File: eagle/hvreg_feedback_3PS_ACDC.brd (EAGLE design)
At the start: 128.5 x 101.9 mm, 14 parts

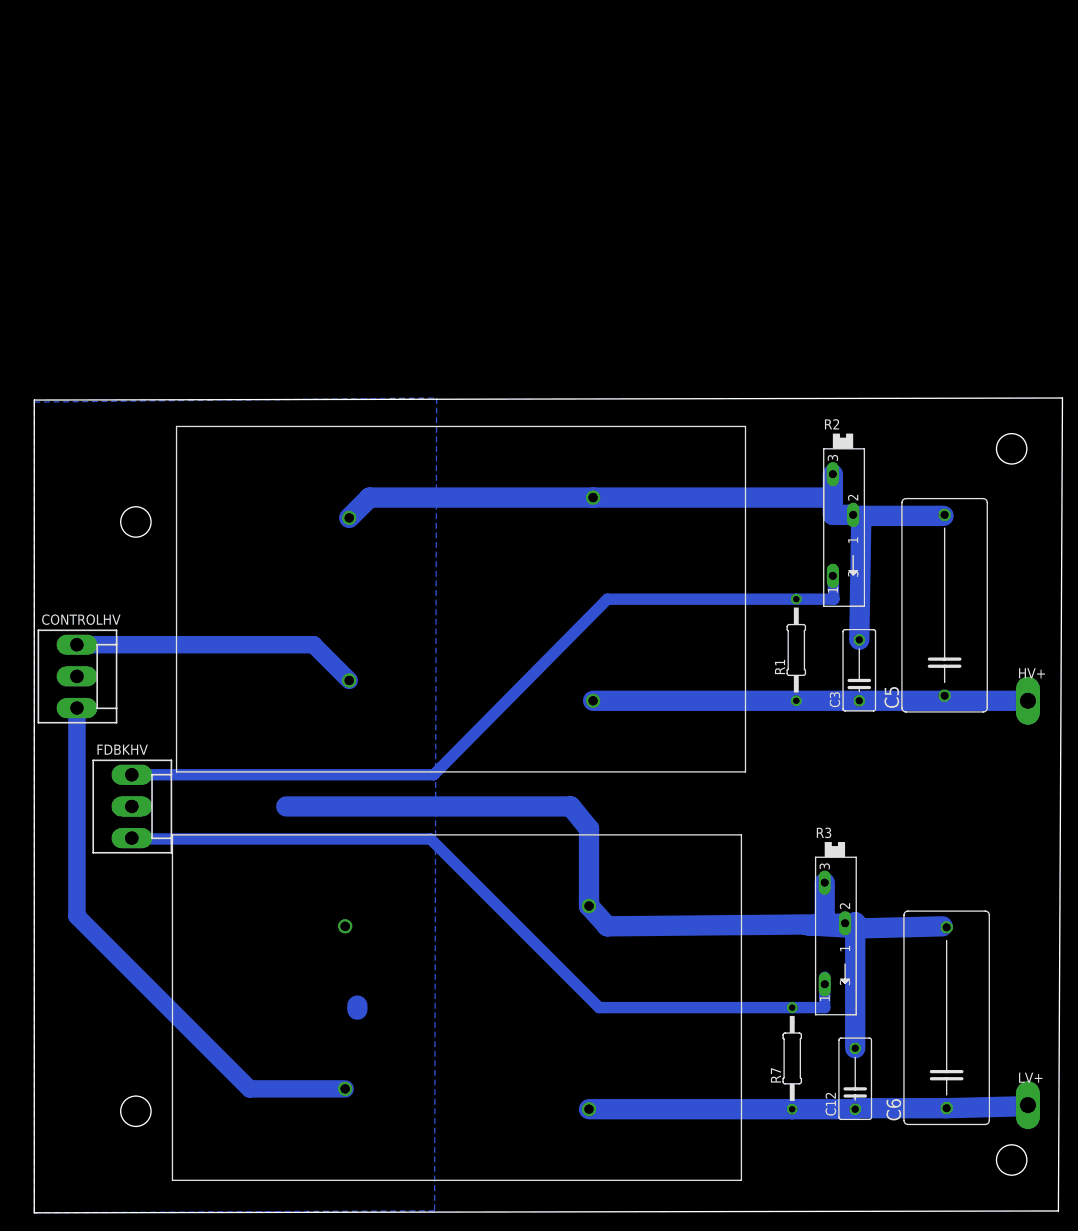
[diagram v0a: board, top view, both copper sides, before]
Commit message: 3PS, 2 1kV in parallel
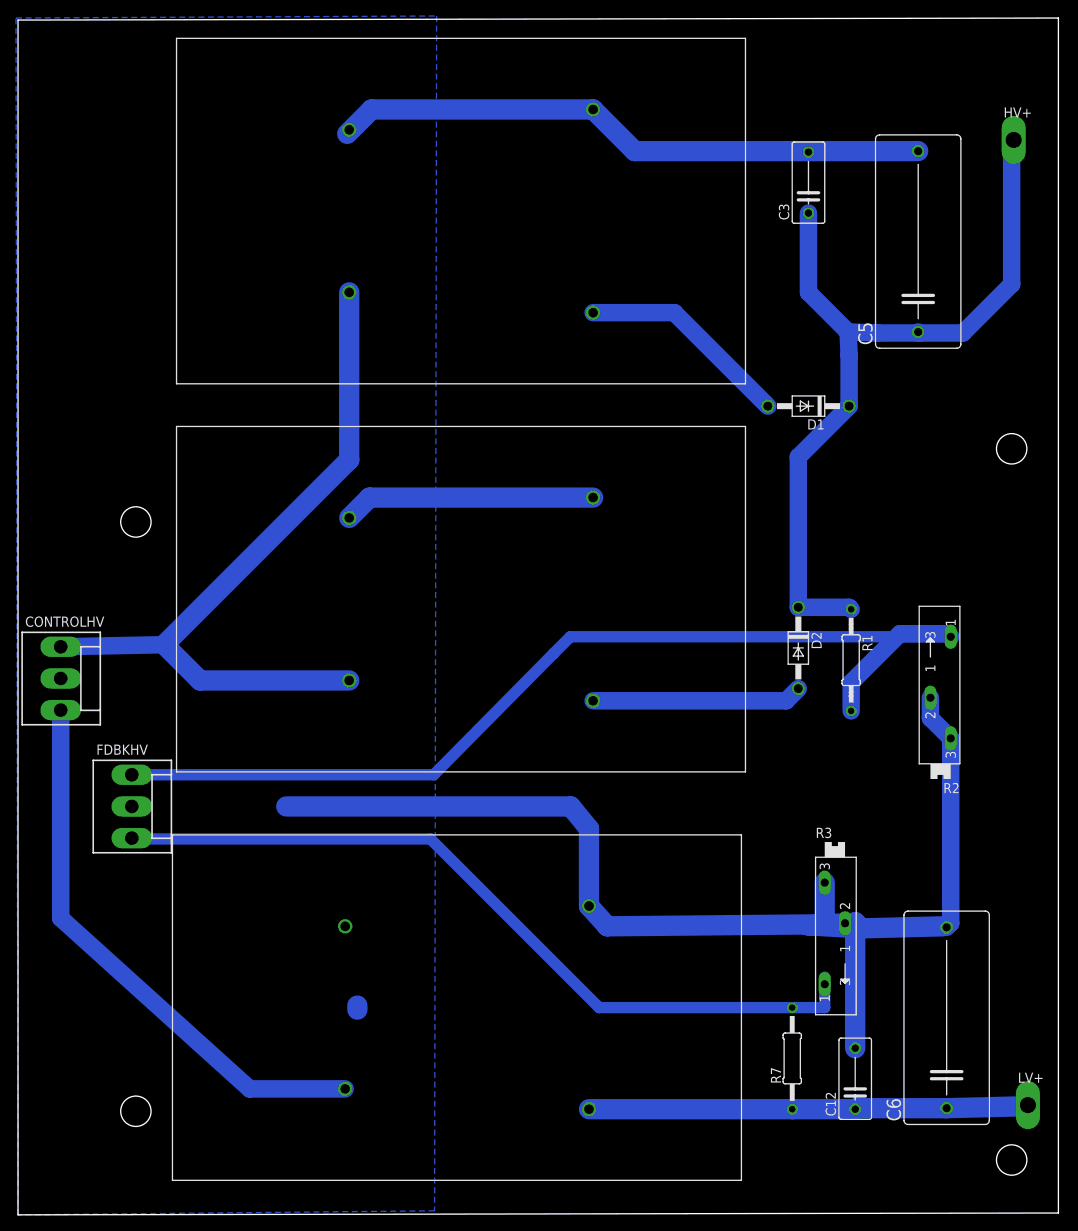
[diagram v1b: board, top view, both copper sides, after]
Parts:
- added D1, D2: 1N4004, diode:DO41-10
- added U$3: EMCO-F104PIN, dc-dc-converter:EMCO-F
- moved HV+ 70.1 mm to (140.2, 133.9)
- moved C3 61.3 mm to (114.6, 128.5)
- moved C5 45.6 mm to (128.3, 121.2)
- moved R2 22.6 mm to (131.1, 66.0), turned to 90 degrees
- moved R1 6.97 mm to (119.9, 68.8), turned to 270 degrees
- moved CONTROLHV 2.05 mm to (21.1, 66.5)
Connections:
- removed net N$1: C3.1, C5.1, HV+.TP, R1.1, U$1.P$3
- new net N$6: D1.A, U$3.P$3
- new net N$7: D2.A, U$1.P$3
- new net N$9: C3.1, C5.1, D1.C, D2.C, HV+.TP, R1.1
- net GND: now also U$3.P$2, U$3.P$4
- net N$4: now also U$3.P$1
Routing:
- net N$9: track 0.00 -> 101.3 mm
- net N$4: track 35.9 -> 91.5 mm
- net N$1: track 54.4 -> 0.00 mm
- net GND: track 222.6 -> 262.7 mm
- net N$3: track 99.8 -> 128.2 mm
- net N$6: track 0.00 -> 26.7 mm
- net N$7: track 0.00 -> 26.3 mm
- net N$5: track 68.5 -> 69.8 mm
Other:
- board size 128.5 x 101.9 mm -> 130 x 149.6 mm

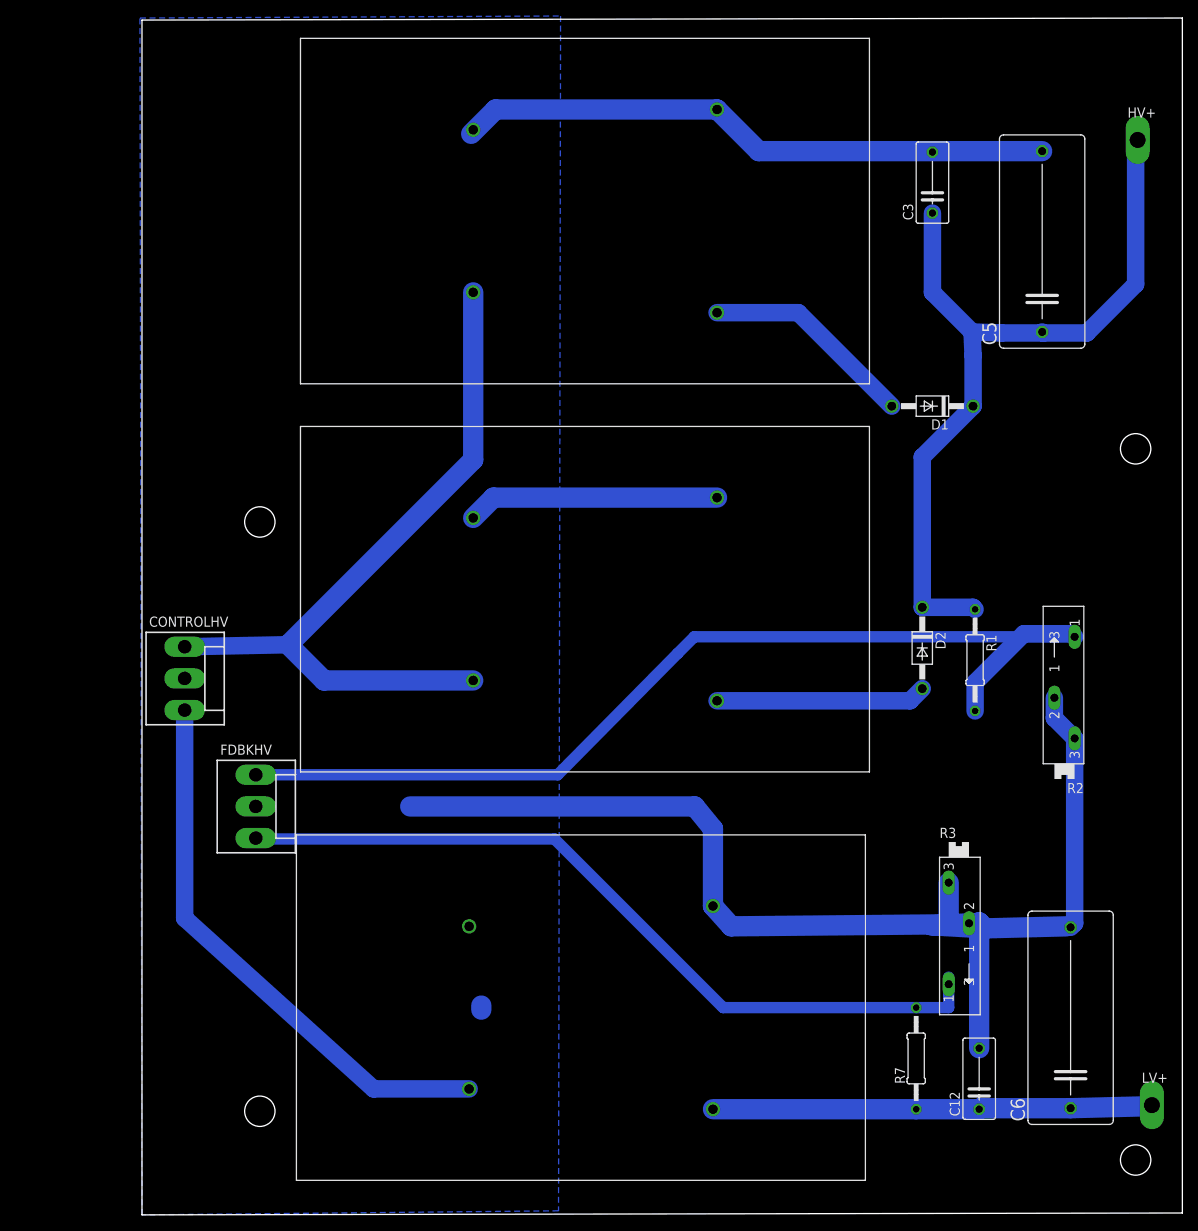
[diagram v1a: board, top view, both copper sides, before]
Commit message: capacitor bank
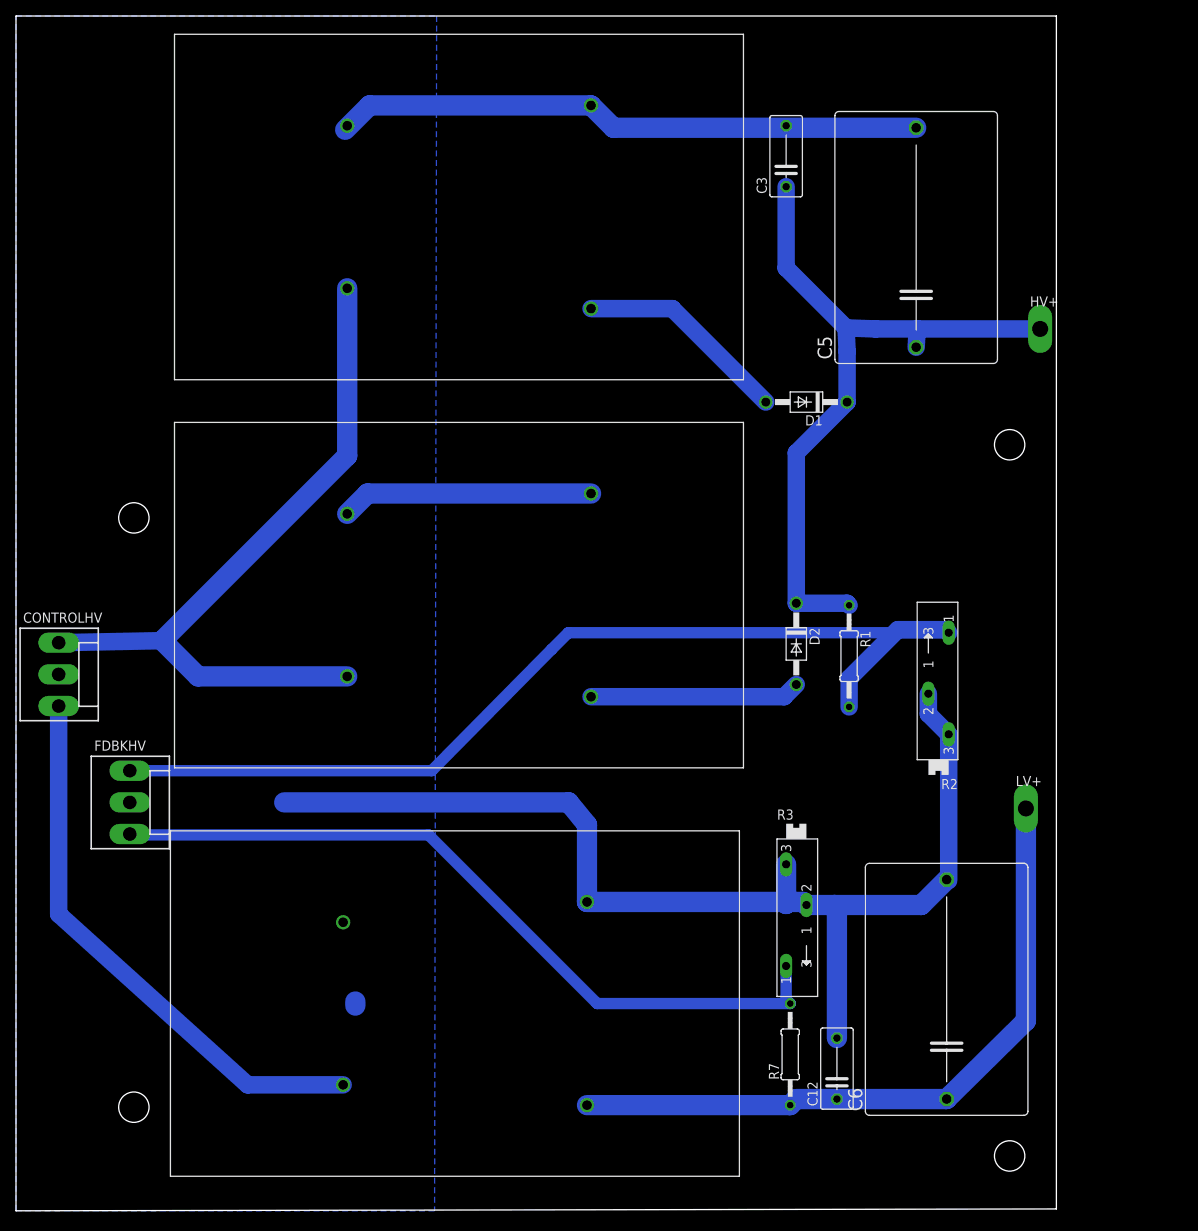
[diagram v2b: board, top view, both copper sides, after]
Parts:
- C5, C6: device rcl:C225-108X268 -> rcl:C275-205X316
- moved LV+ 40.3 mm to (126.2, 50.3)
- moved HV+ 26.6 mm to (128.0, 110.2)
- moved R3 20.4 mm to (97.5, 36.3)
- moved C3 18.6 mm to (96.3, 131.8)
- moved C12 17.8 mm to (102.6, 17.8)
- moved C6 15.9 mm to (116.3, 27.7)
- moved C5 15.8 mm to (112.5, 121.7)
- moved D1 15.8 mm to (98.8, 101.1)
- moved D2 15.8 mm to (97.5, 70.9)
- moved R1 15.8 mm to (104.1, 69.3)
- moved R7 15.8 mm to (96.8, 19.6)
- moved U$2 15.8 mm to (40.9, 15.7)
- moved CONTROLHV 15.8 mm to (5.33, 67.1)
- moved FDBKHV 15.8 mm to (14.2, 51.1)
- moved U$1 15.8 mm to (41.4, 66.8)
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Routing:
- net N$2: track 55.0 -> 85.7 mm
- net GND: track 262.7 -> 247.6 mm
- net N$9: track 101.3 -> 91.1 mm
- net N$8: track 99.5 -> 96.5 mm
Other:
- board size 130 x 149.6 mm -> 130 x 149.4 mm

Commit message: tweaks. still need bigger vias for zeners and hv resistors
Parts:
- added C1, C10, C15, C4: 1n, rcl:C075-042X103
- added C11, C16, C2, C7: 10p, rcl:C075-042X103
- added C13, C8: .01u, rcl:C075-042X103
- added C14, C9: 1u, rcl:C275-205X316
- added D3, D4: 1N4004, diode:DO41-10
- added HV-, LV-: TPPAD1-20Y, testpad:P1-20Y
- added R4, R6: 2M, resistor:0207/12
- added R5, R8: (no value), pot:SP19L
- CONTROLHV, FDBKHV: device con-molex:KK-156-3 -> con-molex:KK-156-4
- U$3: value EMCO-F104PIN -> EMCO-F20CT; device dc-dc-converter:EMCO-F -> dc-dc-converter:EMCO-F*CT
- moved CONTROLHV 217.5 mm to (10.2, -150.4), turned to 0 degrees
- moved FDBKHV 211.6 mm to (10.2, -160.5), turned to 0 degrees
- moved LV+ 178.7 mm to (1.78, -78.0)
- moved D2 149.2 mm to (6.10, -47.0), turned to 0 degrees
- moved U$3 148.6 mm to (21.6, -32.0)
- moved C3 65.4 mm to (109.5, 67.8)
- moved HV+ 54.1 mm to (133.6, 56.4), turned to 90 degrees
- moved D1 49.3 mm to (119.6, 56.4)
- moved C5 45.2 mm to (123.2, 77.7)
- moved R2 26.8 mm to (101.3, 89.4), turned to 270 degrees
- moved R1 11.2 mm to (93.0, 70.6), turned to 90 degrees
- moved R3 9.92 mm to (95.2, 46.0)
- moved C6 9.35 mm to (123.2, 34.0)
- moved R7 8.32 mm to (92.5, 26.7)
- moved C12 7.54 mm to (98.6, 24.1)
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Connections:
- new net N$1: C1.1, C2.1, C3.1, C5.1, D1.A, R1.1, U$1.P$3
- new net N$10: C13.1, C14.1, C15.1, C16.1, D4.C, R6.1
- new net N$11: R6.2, R8.A
- new net N$12: D4.A, LV-.TP
- new net N$13: CONTROLHV.1, U$1.P$1
- new net N$14: CONTROLHV.2, U$3.P$1
- new net N$5: C10.1, C11.1, C8.1, C9.1, D3.A, R4.1
- net GND: now also C1.2, C10.2, C11.2, C13.2, C14.2, C15.2, C16.2, C2.2, C4.2, C7.2, C8.2, C9.2, CONTROLHV.4, FDBKHV.4, R5.E, R5.S, R8.E, R8.S, U$2.P$3, U$3.P$5; no longer CONTROLHV.2, FDBKHV.2, U$2.P$4, U$3.P$4
- net N$2: now also C4.1, C7.1, D2.C, U$2.P$4; no longer LV+.TP, U$2.P$3
- net N$4: now also D2.A, HV-.TP; no longer CONTROLHV.1, U$1.P$1, U$3.P$1
- net N$6: now also D1.C, HV+.TP; no longer D1.A, U$3.P$3
- net N$7: now also FDBKHV.2, R4.2, R5.A; no longer D2.A, U$1.P$3
- net N$9: now also D3.C, LV+.TP; no longer C3.1, C5.1, D1.C, D2.C, HV+.TP, R1.1
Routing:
- net N$4: track 91.5 -> 0.00 mm
- net N$9: track 91.1 -> 0.00 mm
- net N$15: track 69.8 -> 0.00 mm
- net N$3: track 128.2 -> 65.9 mm
- net N$1: track 0.00 -> 61.0 mm
- net N$2: track 85.7 -> 51.5 mm
- net N$7: track 26.3 -> 0.00 mm
- net N$6: track 26.7 -> 10.2 mm
- net GND: track 247.6 -> 258.3 mm
- net N$8: track 96.5 -> 95.1 mm
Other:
- board size 130 x 149.4 mm -> 137.9 x 101.6 mm

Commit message: layout fixes
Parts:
- removed R6: 2M, resistor:0207/12
- removed R8: (no value), pot:SP19L
- C1, C2, C3: device rcl:C075-042X103 -> rcl:C102-043X133
- moved FDBKHV 262.0 mm to (19.3, 101.3), turned to 270 degrees
- moved D4 244.6 mm to (150.9, 76.5), turned to 270 degrees
- moved LV+ 238.3 mm to (151.1, 107.7)
- moved LV- 237.1 mm to (150.9, 58.9)
- moved C15 235.7 mm to (110.5, 78.0), turned to 270 degrees
- moved C16 228.7 mm to (104.1, 78.0), turned to 270 degrees
- moved CONTROLHV 226.3 mm to (8.38, 75.9), turned to 270 degrees
- moved C13 224.0 mm to (117.1, 78.0), turned to 270 degrees
- moved C10 220.5 mm to (104.4, 111.5), turned to 90 degrees
- moved D3 220.0 mm to (151.1, 93.2), turned to 270 degrees
- moved C11 218.8 mm to (111.0, 111.5), turned to 90 degrees
- moved R5 217.3 mm to (86.4, 114.6)
- moved C14 212.7 mm to (131.3, 67.8), turned to 270 degrees
- moved R4 211.8 mm to (111.0, 88.1), turned to 180 degrees
- moved C8 211.4 mm to (117.3, 111.5), turned to 90 degrees
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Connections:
- removed net N$11: R6.2, R8.A
- net GND: no longer R8.E, R8.S
- net N$10: no longer R6.1
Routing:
- net GND: track 258.3 -> 518.8 mm
- net N$7: track 0.00 -> 114.9 mm
- net N$13: track 0.00 -> 87.5 mm
- net N$15: track 0.00 -> 84.6 mm
- net N$5: track 0.00 -> 66.3 mm
- net N$2: track 51.5 -> 110.7 mm
- net N$10: track 0.00 -> 46.8 mm
- net N$3: track 65.9 -> 107.9 mm
- net N$14: track 0.00 -> 41.4 mm
- net N$8: track 95.1 -> 117.2 mm
- net N$4: track 0.00 -> 13.7 mm
- net N$12: track 0.00 -> 13.1 mm
- net N$9: track 0.00 -> 9.40 mm
- net N$1: track 61.0 -> 63.0 mm
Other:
- board size 137.9 x 101.6 mm -> 158.8 x 171.4 mm
